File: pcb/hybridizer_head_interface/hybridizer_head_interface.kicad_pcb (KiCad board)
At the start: 2 copper layers, 85.6 x 132.2 mm, 79 parts, among them P1 HEADER_02X08_SMD, P2 HEADER_02X05_SMD, U1 HALL_DRV5053, U10 MAX4215, U11 HALL_DRV5053, U12 MAX4215, U13 HALL_DRV5053, U14 MAX4215, U2 MAX4215, U3 HALL_DRV5053, U4 MAX4215, U5 HALL_DRV5053, U6 MAX4215, U7 HALL_DRV5053, U8 MAX4215, U9 HALL_DRV5053

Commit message: Made version 1.1 modifications.
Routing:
- net VAA: track 423.8 -> 0.00 mm
- net /OUT0: track 120.9 -> 0.00 mm, vias 3 -> 0
- net +5V: track 361.2 -> 255.6 mm, vias 8 -> 7
- net /A0: track 94.6 -> 0.00 mm, vias 2 -> 0
- net /A2: track 90.7 -> 0.00 mm, vias 2 -> 0
- net /OUT1: track 87.3 -> 0.00 mm, vias 2 -> 0
- net /OUT3: track 76.7 -> 0.00 mm, vias 3 -> 0
- net /OUT7: track 72.3 -> 0.00 mm, vias 1 -> 0
- net /OUT2: track 71.4 -> 0.00 mm, vias 2 -> 0
- net /OUT4: track 69.4 -> 0.00 mm
- net /A3: track 65.0 -> 0.00 mm, vias 2 -> 0
- net /A5: track 59.2 -> 0.00 mm, vias 2 -> 0
- net GND: track 388.3 -> 332.4 mm, vias 8 -> 7
- net /A6: track 55.5 -> 0.00 mm, vias 2 -> 0
- net /A1: track 52.6 -> 0.00 mm, vias 2 -> 0
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- removed copper zone on F.Cu, net +5V
- removed copper zone on B.Cu, net GND
- removed copper zone on F.Cu, net VAA

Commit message: Progress towards hybridizer_head_interface_v1.1.
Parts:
- added C22: 1uF, hybridizer_head_interface:SM0805_POL, F.Cu at (89.2, 104.5)
- added C23: 1uF, hybridizer_head_interface:SM0805_POL, F.Cu at (95.5, 34.7)
- added C24: 1uF, hybridizer_head_interface:SM0805_POL, F.Cu at (95.5, 53.1)
- added C25: 1uF, hybridizer_head_interface:SM0805_POL, F.Cu at (95.5, 71.5)
- added C26: 10nF, hybridizer_head_interface:SM0402, F.Cu at (91.7, 97.5)
- added C27: 10nF, hybridizer_head_interface:SM0402, F.Cu at (88.5, 31.5)
- added C28: 10nF, hybridizer_head_interface:SM0402, F.Cu at (88.5, 49.9)
- added C29: 10nF, hybridizer_head_interface:SM0402, F.Cu at (88.5, 68.3)
- added C30: 1uF, hybridizer_head_interface:SM0805_POL, F.Cu at (91.7, 36.6)
- added C31: 1uF, hybridizer_head_interface:SM0805_POL, F.Cu at (91.7, 55.0)
- added C32: 1uF, hybridizer_head_interface:SM0805_POL, F.Cu at (91.7, 73.4)
- added C33: 1uF, hybridizer_head_interface:SM0805_POL, F.Cu at (91.1, 91.2)
- added C34: 10nF, hybridizer_head_interface:SM0402, F.Cu at (98.7, 39.8)
- added C35: 10nF, hybridizer_head_interface:SM0402, F.Cu at (98.7, 58.2)
- added C36: 10nF, hybridizer_head_interface:SM0402, F.Cu at (98.7, 76.6)
- added C37: 10nF, hybridizer_head_interface:SM0402, F.Cu at (94.2, 84.2)
- added D10: diode_schottky_20V_1A, hybridizer_head_interface:SM0805_POL, F.Cu at (101.2, 31.5)
- added D11: diode_schottky_20V_1A, hybridizer_head_interface:SM0805_POL, F.Cu at (101.2, 49.9)
- added D12: diode_schottky_20V_1A, hybridizer_head_interface:SM0805_POL, F.Cu at (101.2, 68.3)
- added D13: diode_schottky_20V_1A, hybridizer_head_interface:SM0805_POL, F.Cu at (86.0, 39.8)
- added D14: diode_schottky_20V_1A, hybridizer_head_interface:SM0805_POL, F.Cu at (86.0, 58.2)
- added D15: diode_schottky_20V_1A, hybridizer_head_interface:SM0805_POL, F.Cu at (86.0, 76.6)
- added D16: diode_schottky_20V_1A, hybridizer_head_interface:SM0805_POL, F.Cu at (95.5, 96.9)
- added D9: diode_schottky_20V_1A, hybridizer_head_interface:SM0805_POL, F.Cu at (92.3, 109.6)
- added R10: 300, hybridizer_head_interface:SM0402, F.Cu at (123.2, 70.9)
- added R11: 300, hybridizer_head_interface:SM0402, F.Cu at (123.2, 108.3)
- added R12: 300, hybridizer_head_interface:SM0402, F.Cu at (64.0, 33.4)
- added R13: 300, hybridizer_head_interface:SM0402, F.Cu at (64.0, 70.9)
- added R14: 300, hybridizer_head_interface:SM0402, F.Cu at (64.0, 108.3)
- added R15: 300, hybridizer_head_interface:SM0402, F.Cu at (55.5, 118.5)
- added R16: 205k, hybridizer_head_interface:SM0402, F.Cu at (91.7, 99.5)
- added R17: 110k, hybridizer_head_interface:SM0402, F.Cu at (91.7, 95.6)
- added R18: 205k, hybridizer_head_interface:SM0402, F.Cu at (90.4, 31.5)
- added R19: 110k, hybridizer_head_interface:SM0402, F.Cu at (86.6, 31.5)
- added R20: 205k, hybridizer_head_interface:SM0402, F.Cu at (90.4, 49.9)
- added R21: 110k, hybridizer_head_interface:SM0402, F.Cu at (86.6, 49.9)
- added R22: 205k, hybridizer_head_interface:SM0402, F.Cu at (90.4, 68.3)
- added R23: 110k, hybridizer_head_interface:SM0402, F.Cu at (86.6, 68.3)
- added R24: 205k, hybridizer_head_interface:SM0402, F.Cu at (96.8, 39.8)
- added R25: 110k, hybridizer_head_interface:SM0402, F.Cu at (100.6, 39.8)
- added R26: 205k, hybridizer_head_interface:SM0402, F.Cu at (96.8, 58.2)
- added R27: 110k, hybridizer_head_interface:SM0402, F.Cu at (100.6, 58.2)
- added R28: 205k, hybridizer_head_interface:SM0402, F.Cu at (96.8, 76.6)
- added R29: 110k, hybridizer_head_interface:SM0402, F.Cu at (100.6, 76.6)
- added R30: 205k, hybridizer_head_interface:SM0402, F.Cu at (94.2, 86.1)
- added R31: 137k, hybridizer_head_interface:SM0402, F.Cu at (94.2, 82.3)
- added R8: 300, hybridizer_head_interface:SM0402, F.Cu at (131.7, 118.5)
- added R9: 300, hybridizer_head_interface:SM0402, F.Cu at (123.2, 33.4)
- added U15: DRV103, hybridizer_head_interface:SOIC_8, F.Cu at (93.6, 104.5)
- added U16: DRV103, hybridizer_head_interface:SOIC_8, F.Cu at (95.5, 30.2)
- added U17: DRV103, hybridizer_head_interface:SOIC_8, F.Cu at (95.5, 48.7)
- added U18: DRV103, hybridizer_head_interface:SOIC_8, F.Cu at (95.5, 67.1)
- added U19: DRV103, hybridizer_head_interface:SOIC_8, F.Cu at (91.7, 41.0)
- added U20: DRV103, hybridizer_head_interface:SOIC_8, F.Cu at (91.7, 59.4)
- added U21: DRV103, hybridizer_head_interface:SOIC_8, F.Cu at (91.7, 77.9)
- added U22: DRV103, hybridizer_head_interface:SOIC_8, F.Cu at (95.5, 91.2)
- D1, D2, D3, D4, D5, D6, D7, D8: value LED_24V_SMD -> LED_0805; footprint hybridizer_head_interface:LED_555-3XXX_SMD -> hybridizer_head_interface:LED0805
- P1: value HEADER_02X08_SMD -> HEADER_02X07_SMD; footprint hybridizer_head_interface:HEADER_02x08_SMD -> hybridizer_head_interface:HEADER_02x07_SMD
- moved C15 12.7 mm to (71.4, 56.3)
- moved C6 12.7 mm to (115.8, 56.3)
- moved C12 12.7 mm to (108.8, 102.0)
- moved C21 12.0 mm to (79.0, 102.0)
- moved R1 3.81 mm to (93.6, 125.5)
- moved D1 1.27 mm to (128.5, 118.5), turned to 180 degrees
- moved D8 1.27 mm to (58.7, 118.5), turned to 0 degrees
- moved C2 1.27 mm to (93.6, 121.7)
- turned D2 to 270 degrees
- turned D3 to 270 degrees
- turned D4 to 270 degrees
- turned D5 to 270 degrees
- turned D6 to 270 degrees
- turned D7 to 270 degrees
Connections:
- D1 pad 1: VAA -> Net-(D1-Pad1)
- D1 pad 2: /OUT0 -> GND
- D2 pad 1: VAA -> Net-(D2-Pad1)
- D2 pad 2: /OUT1 -> GND
- D3 pad 1: VAA -> Net-(D3-Pad1)
- D3 pad 2: /OUT2 -> GND
- D4 pad 1: VAA -> Net-(D4-Pad1)
- D4 pad 2: /OUT3 -> GND
- D5 pad 1: VAA -> Net-(D5-Pad1)
- D5 pad 2: /OUT4 -> GND
- D6 pad 1: VAA -> Net-(D6-Pad1)
- D6 pad 2: /OUT5 -> GND
- D7 pad 1: VAA -> Net-(D7-Pad1)
- D7 pad 2: /OUT6 -> GND
- D8 pad 1: VAA -> Net-(D8-Pad1)
- D8 pad 2: /OUT7 -> GND
- P1 pad 10: /OUT4 -> /IO3
- P1 pad 11: VAA -> /IO4
- P1 pad 12: /OUT5 -> /IO5
- P1 pad 13: VAA -> /IO6
- P1 pad 14: /OUT6 -> /IO7
- P1 pad 2: /OUT0 -> GND
- P1 pad 4: /OUT1 -> GND
- P1 pad 5: VAA -> Net-(P1-Pad5)
- P1 pad 6: /OUT2 -> GND
- P1 pad 7: VAA -> /IO0
- P1 pad 8: /OUT3 -> /IO1
- P1 pad 9: VAA -> /IO2
- P2 pad 2: GND -> Net-(P2-Pad2)
- S1 pad 1: VAA -> /SH0
- S1 pad 2: /OUT0 -> GND
- S2 pad 1: VAA -> /SH1
- S2 pad 2: /OUT1 -> GND
- S3 pad 1: VAA -> /SH2
- S3 pad 2: /OUT2 -> GND
- S4 pad 1: VAA -> /SH3
- S4 pad 2: /OUT3 -> GND
- S5 pad 1: VAA -> /SH4
- S5 pad 2: /OUT4 -> GND
- S6 pad 1: VAA -> /SH5
- S6 pad 2: /OUT5 -> GND
- S7 pad 1: VAA -> /SH6
- S7 pad 2: /OUT6 -> GND
- S8 pad 1: VAA -> /SH7
- S8 pad 2: /OUT7 -> GND
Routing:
- net GND: track 332.4 -> 165.8 mm
- net +5V: track 255.6 -> 96.0 mm
- net VAA: track 0.00 -> 51.0 mm
- net Net-(R1-Pad2): track 16.6 -> 0.00 mm, vias 1 -> 0
- net Net-(C2-Pad1): track 11.2 -> 7.35 mm
- net /SH7: track 0.00 -> 3.38 mm
- net /SH3: track 0.00 -> 3.19 mm
- net /SH2: track 0.00 -> 3.19 mm
- net /SH5: track 0.00 -> 3.19 mm
- net /SH6: track 0.00 -> 3.19 mm
- net /SH0: track 0.00 -> 2.56 mm
- net Net-(D7-Pad1): track 0.00 -> 1.77 mm
- net Net-(D4-Pad1): track 0.00 -> 1.77 mm
- net Net-(D6-Pad1): track 0.00 -> 1.67 mm
- net Net-(D3-Pad1): track 0.00 -> 1.67 mm
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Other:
- board text added: "hybridizer_head_interface Janelia Research Campus 05/2015 version 1.1 J005165"
- board text removed: "hybridizer_head_interface Janelia Research Campus 04/2015 version 1.0 J005165"

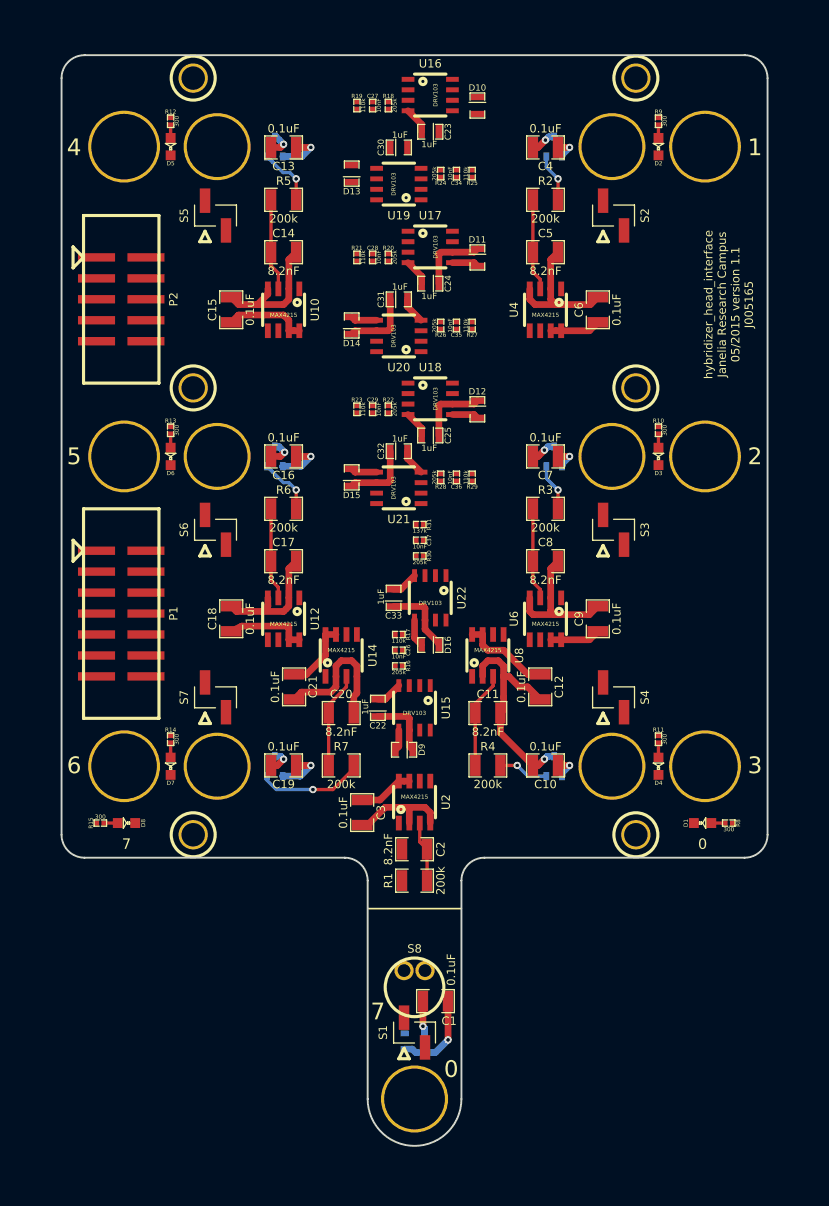
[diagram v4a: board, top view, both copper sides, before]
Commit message: Finished hybridizer_head_interface pcb v1.1.
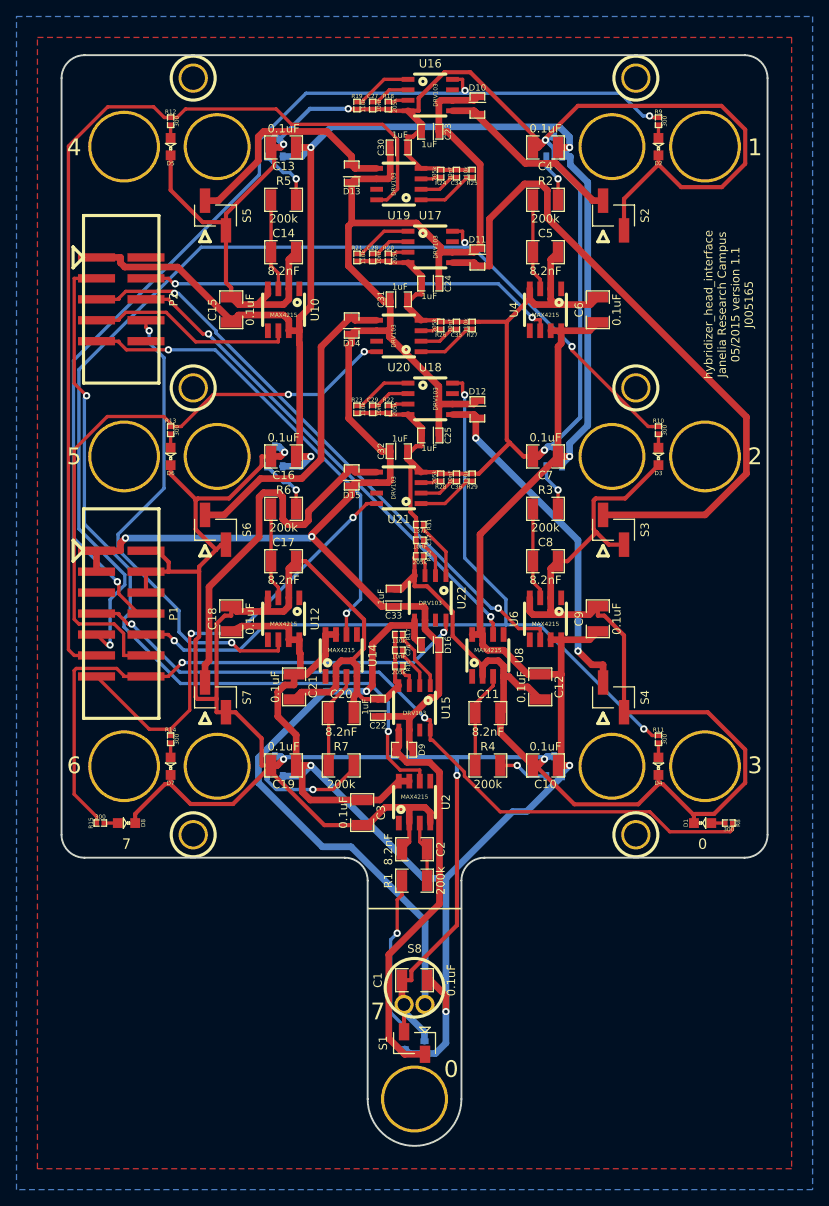
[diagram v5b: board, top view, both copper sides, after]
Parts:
- S1: value HEADER_01X02_SMD -> HEADER_01X02_SMD_N; footprint hybridizer_head_interface:Header_2_Pin_SMD -> hybridizer_head_interface:Header_2_Pin_SMD_N
- U1, U11, U13, U3, U5, U7, U9: value HALL_DRV5053 -> HALL_DRV5053_OA_-73mT
- moved S8 4.11 mm to (93.6, 140.5), turned to 180 degrees
- moved C1 3.59 mm to (93.6, 137.6)
- moved S1 1.27 mm to (93.6, 145.2), turned to 0 degrees
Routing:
- net GND: track 165.8 -> 756.3 mm, vias 7 -> 8
- net +5V: track 96.0 -> 375.7 mm
- net VAA: track 51.0 -> 206.1 mm, vias 0 -> 2
- net /IO2: track 0.00 -> 127.6 mm, vias 0 -> 3
- net /IO1: track 0.00 -> 125.9 mm, vias 0 -> 3
- net /IO4: track 0.00 -> 118.2 mm
- net /IO3: track 0.00 -> 102.5 mm, vias 0 -> 3
- net /A0: track 0.00 -> 96.8 mm, vias 0 -> 2
- net /IO0: track 0.00 -> 90.8 mm, vias 0 -> 2
- net /SH2: track 3.19 -> 83.3 mm
- net /IO5: track 0.00 -> 75.6 mm, vias 0 -> 2
- net /A2: track 0.00 -> 72.7 mm, vias 0 -> 2
- net /IO7: track 0.00 -> 68.8 mm, vias 0 -> 2
- net /SH7: track 3.38 -> 72.2 mm, vias 0 -> 1
- net /A3: track 0.00 -> 60.1 mm, vias 0 -> 2
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- added copper zone on B.Cu, net GND
- added copper zone on F.Cu, net GND

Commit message: Schematic changes towards hybridizer_head_interface v1.2.
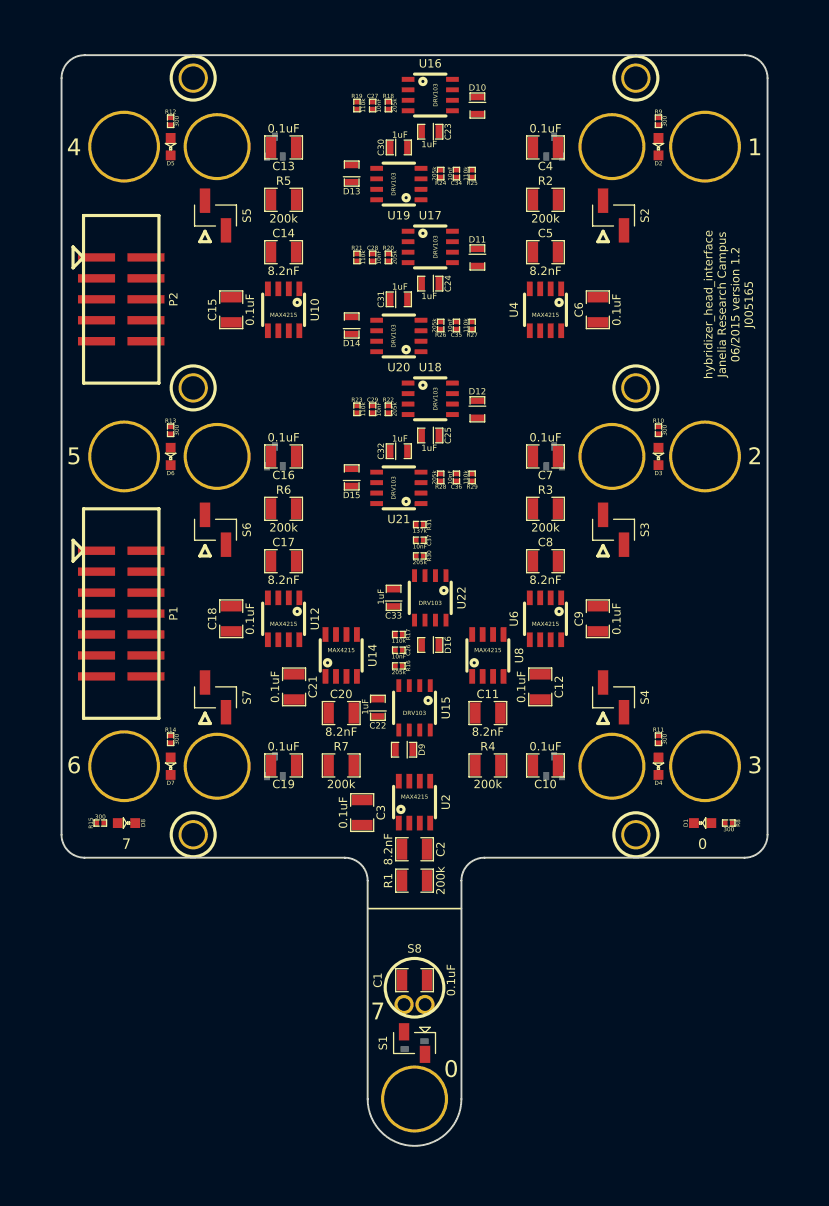
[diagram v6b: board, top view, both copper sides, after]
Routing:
- net GND: track 756.3 -> 0.00 mm, vias 8 -> 0
- net +5V: track 375.7 -> 0.00 mm, vias 7 -> 0
- net VAA: track 206.1 -> 0.00 mm, vias 2 -> 0
- net /IO2: track 127.6 -> 0.00 mm, vias 3 -> 0
- net /IO1: track 125.9 -> 0.00 mm, vias 3 -> 0
- net /IO4: track 118.2 -> 0.00 mm
- net /IO3: track 102.5 -> 0.00 mm, vias 3 -> 0
- net /A0: track 96.8 -> 0.00 mm, vias 2 -> 0
- net /IO0: track 90.8 -> 0.00 mm, vias 2 -> 0
- net /SH2: track 83.3 -> 0.00 mm
- net /IO5: track 75.6 -> 0.00 mm, vias 2 -> 0
- net /A2: track 72.7 -> 0.00 mm, vias 2 -> 0
- net /SH7: track 72.2 -> 0.00 mm, vias 1 -> 0
- net /IO7: track 68.8 -> 0.00 mm, vias 2 -> 0
- net /A3: track 60.1 -> 0.00 mm, vias 2 -> 0
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- removed copper zone on B.Cu, net GND
- removed copper zone on F.Cu, net GND
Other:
- board text added: "hybridizer_head_interface Janelia Research Campus 06/2015 version 1.2 J005165"
- board text removed: "hybridizer_head_interface Janelia Research Campus 05/2015 version 1.1 J005165"

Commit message: Progress towards hybridizer_head_interface_v1.2.
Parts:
- removed C11, C14, C17, C2, C20, C5, C8: 8.2nF, hybridizer_head_interface:SM1210
- removed C12, C15, C18, C21, C3, C6, C9: 0.1uF, hybridizer_head_interface:SM1210
- removed R1, R2, R3, R4, R5, R6, R7: 200k, hybridizer_head_interface:SM1210
- removed U10, U12, U14, U2, U4, U6, U8: MAX4215, hybridizer_head_interface:SOIC_8_N
- added C38: 0.1uF, hybridizer_head_interface:SM1210, F.Cu at (93.6, 125.5)
- added C39: 0.1uF, hybridizer_head_interface:SM1210, F.Cu at (109.5, 37.9)
- added C40: 0.1uF, hybridizer_head_interface:SM1210, F.Cu at (109.5, 75.3)
- added C41: 0.1uF, hybridizer_head_interface:SM1210, F.Cu at (109.5, 112.8)
- added C42: 0.1uF, hybridizer_head_interface:SM1210, F.Cu at (77.7, 37.9)
- added C43: 0.1uF, hybridizer_head_interface:SM1210, F.Cu at (77.7, 75.3)
- added C44: 0.1uF, hybridizer_head_interface:SM1210, F.Cu at (77.7, 112.8)
- added C45: 22uF, hybridizer_head_interface:SM1210_POL, F.Cu at (69.5, 96.3)
- added C46: 10uF, hybridizer_head_interface:SM1210, F.Cu at (69.5, 89.9)
- added C47: 22uF, hybridizer_head_interface:SM1210_POL, F.Cu at (117.7, 89.9)
- added C48: 10uF, hybridizer_head_interface:SM1210, F.Cu at (117.7, 96.3)
- added P3: HEADER_02X05_SMD, hybridizer_head_interface:HEADER_02x05_SMD, F.Cu at (129.2, 55.0)
- added U23: OA, hybridizer_head_interface:SOT-23-3, B.Cu at (91.8, 145.0)
- added U24: OA, hybridizer_head_interface:SOT-23-3, B.Cu at (110.5, 38.3)
- added U25: OA, hybridizer_head_interface:SOT-23-3, B.Cu at (110.5, 75.8)
- added U26: OA, hybridizer_head_interface:SOT-23-3, B.Cu at (110.5, 113.4)
- added U27: OA, hybridizer_head_interface:SOT-23-3, B.Cu at (76.7, 38.3)
- added U28: OA, hybridizer_head_interface:SOT-23-3, B.Cu at (76.7, 75.8)
- added U29: OA, hybridizer_head_interface:SOT-23-3, B.Cu at (76.7, 113.4)
- U1, U11, U13, U3, U5, U7, U9: value HALL_DRV5053_OA_-73mT -> VA
- moved P2 80.7 mm to (129.2, 93.1), turned to 270 degrees
- moved C13 1.91 mm to (77.7, 34.7)
- moved C16 1.91 mm to (77.7, 72.1)
- moved C4 1.91 mm to (109.5, 34.7)
- moved C7 1.91 mm to (109.5, 72.1)
- moved C10 1.90 mm to (109.5, 109.6)
- moved C19 1.90 mm to (77.7, 109.6)
- moved U13 1.78 mm to (76.7, 109.8)
- moved U7 1.78 mm to (110.5, 109.8)
- moved U11 1.78 mm to (76.7, 72.3)
- moved U5 1.78 mm to (110.5, 72.3)
- moved U1 1.78 mm to (95.4, 145.0)
- moved U3 1.78 mm to (110.5, 34.7)
- moved U9 1.78 mm to (76.7, 34.7)
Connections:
- C1 pad 2: GND -> GNDA
- C10 pad 2: GND -> GNDA
- C13 pad 2: GND -> GNDA
- C16 pad 2: GND -> GNDA
- C19 pad 2: GND -> GNDA
- C4 pad 2: GND -> GNDA
- C7 pad 2: GND -> GNDA
- P2 pad 2: Net-(P2-Pad2) -> GNDA
- S1 pad 1: /SH0 -> VAA
- S1 pad 2: GND -> /SH0
- S2 pad 1: /SH1 -> VAA
- S2 pad 2: GND -> /SH1
- S3 pad 1: /SH2 -> VAA
- S3 pad 2: GND -> /SH2
- S4 pad 1: /SH3 -> VAA
- S4 pad 2: GND -> /SH3
- S5 pad 1: /SH4 -> VAA
- S5 pad 2: GND -> /SH4
- S6 pad 1: /SH5 -> VAA
- S6 pad 2: GND -> /SH5
- S7 pad 1: /SH6 -> VAA
- S7 pad 2: GND -> /SH6
- S8 pad 1: /SH7 -> VAA
- S8 pad 2: GND -> /SH7
- U1 pad 2: Net-(R1-Pad2) -> /A0
- U1 pad 3: GND -> GNDA
- U11 pad 2: Net-(R6-Pad2) -> /A5
- U11 pad 3: GND -> GNDA
- U13 pad 2: Net-(R7-Pad2) -> /A6
- U13 pad 3: GND -> GNDA
- U3 pad 2: Net-(R2-Pad2) -> /A1
- U3 pad 3: GND -> GNDA
- U5 pad 2: Net-(R3-Pad2) -> /A2
- U5 pad 3: GND -> GNDA
- U7 pad 2: Net-(R4-Pad2) -> /A3
- U7 pad 3: GND -> GNDA
- U9 pad 2: Net-(R5-Pad2) -> /A4
- U9 pad 3: GND -> GNDA
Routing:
- net GND: track 0.00 -> 5.08 mm
- net VAA: track 0.00 -> 2.54 mm

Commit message: Finished hybridizer_head_interface_v1.2.
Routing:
- net GND: track 5.08 -> 487.3 mm, vias 0 -> 7
- net VAA: track 2.54 -> 408.7 mm
- net GNDA: track 0.00 -> 390.6 mm, vias 0 -> 15
- net +5V: track 0.00 -> 360.5 mm, vias 0 -> 16
- net /IO1: track 0.00 -> 161.5 mm
- net /IO4: track 0.00 -> 119.2 mm
- net /A8: track 0.00 -> 118.7 mm, vias 0 -> 1
- net /A4: track 0.00 -> 116.7 mm, vias 0 -> 1
- net /IO2: track 0.00 -> 113.8 mm, vias 0 -> 2
- net /A14: track 0.00 -> 102.6 mm, vias 0 -> 1
- net /IO3: track 0.00 -> 100.0 mm, vias 0 -> 2
- net /IO0: track 0.00 -> 93.9 mm, vias 0 -> 3
- net /A1: track 0.00 -> 89.2 mm, vias 0 -> 1
- net /IO5: track 0.00 -> 76.5 mm, vias 0 -> 2
- net /A0: track 0.00 -> 73.8 mm, vias 0 -> 1
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- added copper zone on F.Cu, net GND
- added copper zone on B.Cu, net GNDA
